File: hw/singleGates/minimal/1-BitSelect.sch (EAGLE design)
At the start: 15 parts, among them Q1 BC817, Q2 BC817, Q3 BC817, Q4 BC817, Q5 BC817, Q6 BC817

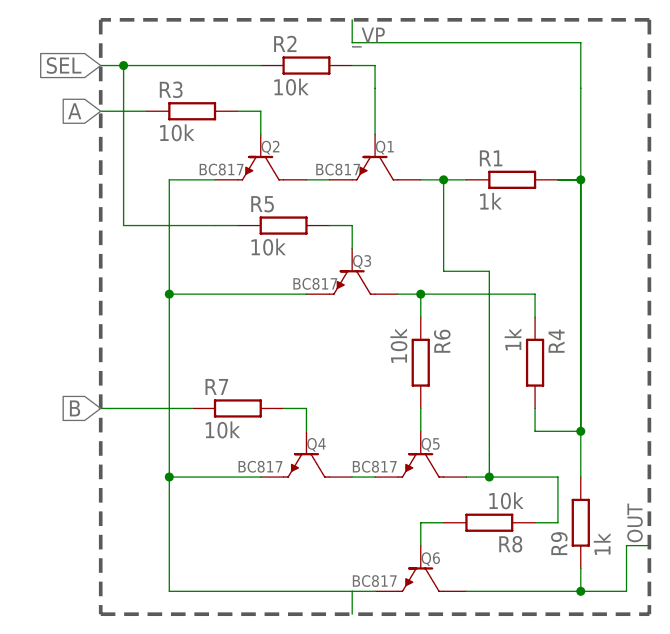
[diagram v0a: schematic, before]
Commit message: Add led output and prepare first alu slice
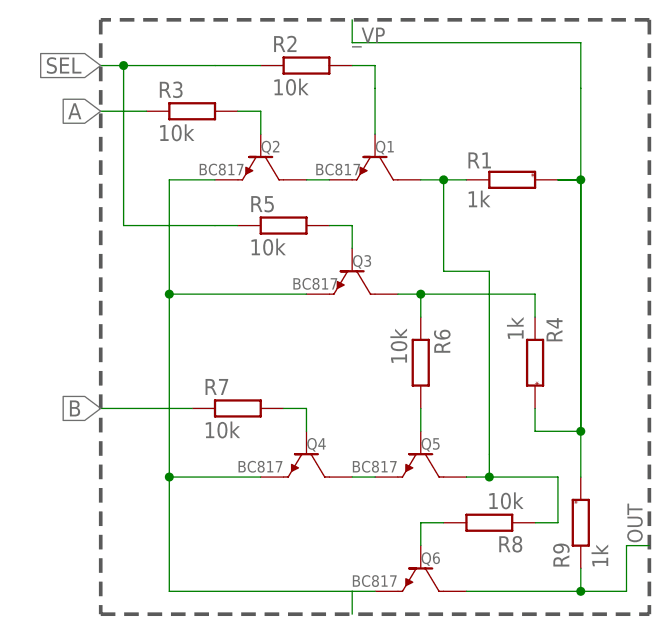
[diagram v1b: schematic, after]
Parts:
- R1, R4, R9: device p.peter-gator:R-EU_R0603 -> p.peter-rcl:R-EU-MARKEDR0603
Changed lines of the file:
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@@
 <part name="R2" library="p.peter-gator" deviceset="R-EU_" device="R0603" value="10k"/>
 <part name="R3" library="p.peter-gator" deviceset="R-EU_" device="R0603" value="10k"/>
-<part name="R1" library="p.peter-gator" deviceset="R-EU_" device="R0603" value="1k"/>
+<part name="R1" library="p.peter-rcl" deviceset="R-EU-MARKED" device="R0603" value="1k"/>
 <part name="R6" library="p.peter-gator" deviceset="R-EU_" device="R0603" value="10k"/>
 <part name="R7" library="p.peter-gator" deviceset="R-EU_" device="R0603" value="10k"/>
-<part name="R9" library="p.peter-gator" deviceset="R-EU_" device="R0603" value="1k"/>
+<part name="R9" library="p.peter-rcl" deviceset="R-EU-MARKED" device="R0603" value="1k"/>
 <part name="R8" library="p.peter-gator" deviceset="R-EU_" device="R0603" value="10k"/>
-<part name="R4" library="p.peter-gator" deviceset="R-EU_" device="R0603" value="1k"/>
+<part name="R4" library="p.peter-rcl" deviceset="R-EU-MARKED" device="R0603" value="1k"/>
 <part name="R5" library="p.peter-gator" deviceset="R-EU_" device="R0603" value="10k"/>
 <part name="Q1" library="p.peter-gator" deviceset="TRANSISTOR-NPN-GENERIC" device="-SOT23-BEC" technology="DEFAULT" value="BC817"/>
